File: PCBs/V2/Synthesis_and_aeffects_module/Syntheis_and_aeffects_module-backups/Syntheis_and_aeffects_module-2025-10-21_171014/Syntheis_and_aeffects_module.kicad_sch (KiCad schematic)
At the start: 36 parts, among them J1(AudioJack)1 Conn_01x03, J2(IN)1 IN, J3(OUT)1 OUT, U1 STM32H750VBTx, U2 TPA6110A2DGN

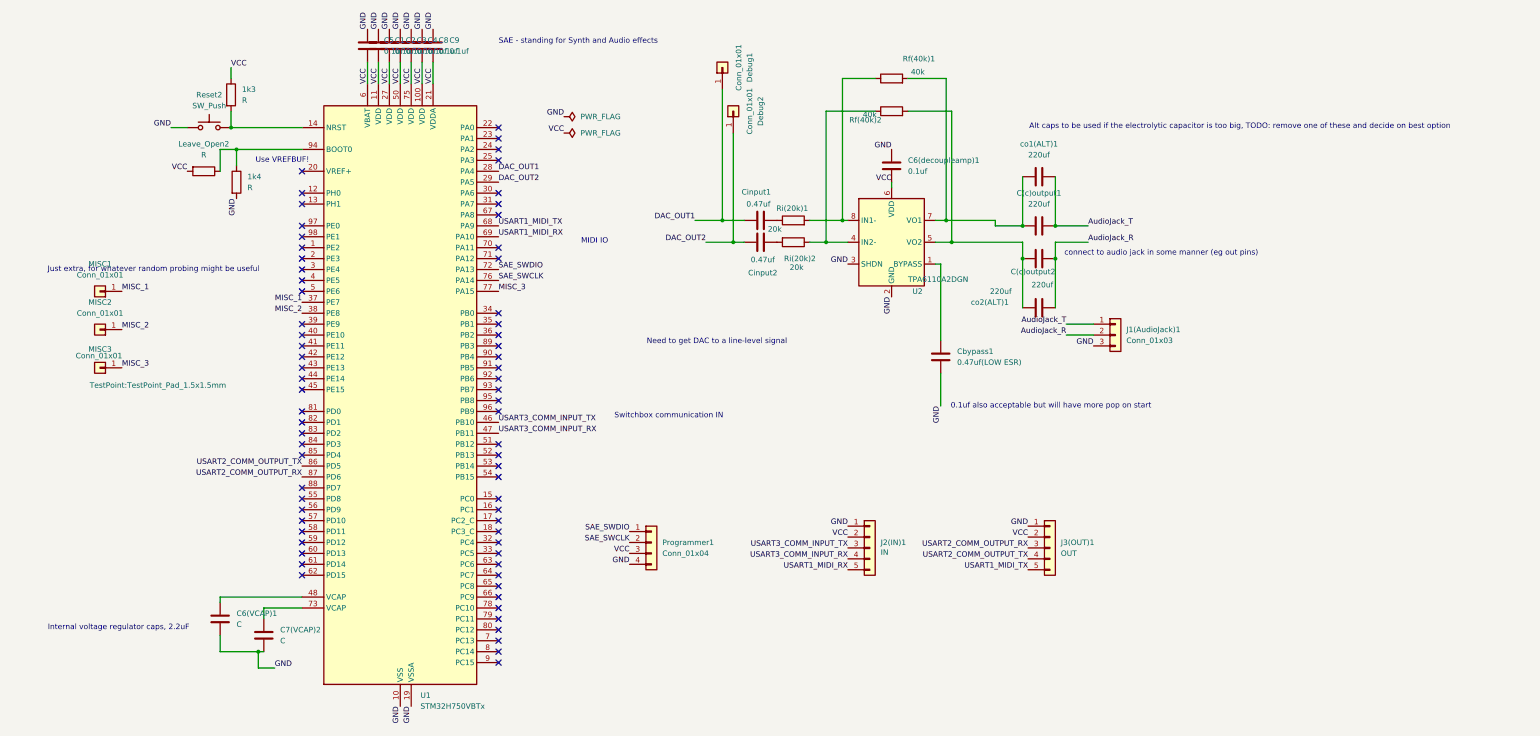
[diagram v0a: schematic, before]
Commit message: testing and fixing PCBs, reordered
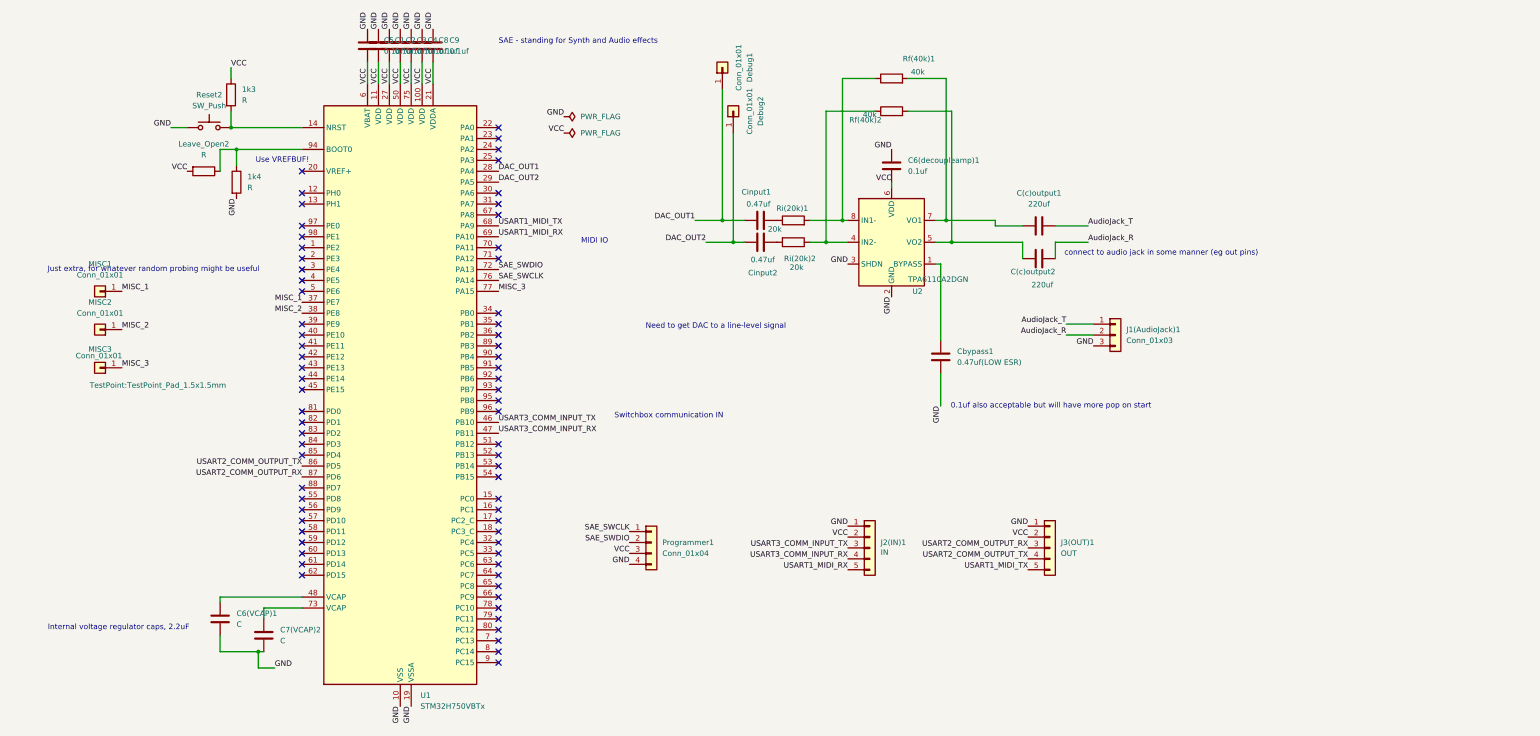
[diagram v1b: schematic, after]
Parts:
- removed co1(ALT)1, co2(ALT)1: 220uf, Capacitor_SMD:C_1206_3216Metric_Pad1.33x1.80mm_HandSolder, symbol Device:C
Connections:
- net SAE_SWCLK: now also Programmer1.1 (Pin_1); no longer Programmer1.2 (Pin_2)
- net SAE_SWDIO: now also Programmer1.2 (Pin_2); no longer Programmer1.1 (Pin_1)
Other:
- note removed: "Alt caps to be used if the electrolytic capacitor is too big, TODO: remove one of these and decide on best option"
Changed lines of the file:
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@@
 	(text "Need to get DAC to a line-level signal"
 		(exclude_from_sim no)
-		(at 176.53 96.774 0)
+		(at 176.276 93.218 0)
 		(effects
 			(font
@@
 		)
 	)
-	(text "Alt caps to be used if the electrolytic capacitor is too big, TODO: remove one of these and decide on best option\n"
-		(exclude_from_sim no)
-		(at 298.196 46.736 0)
-		(effects
-			(font
-				(size 1.27 1.27)
-			)
-		)
-	)
 	(text "Use VREFBUF!\n"
 		(exclude_from_sim no)
@@
 	)
 	(junction
-		(at 255.27 69.85)
-		(diameter 0)
-		(color 0 0 0 0)
-	)
-	(junction
 		(at 63.5 46.99)
 		(diameter 0)
@@
 	)
 	(junction
-		(at 255.27 77.47)
-		(diameter 0)
-		(color 0 0 0 0)
-	)
-	(junction
-		(at 247.65 77.47)
-		(diameter 0)
-		(color 0 0 0 0)
-	)
-	(junction
-		(at 247.65 69.85)
-		(diameter 0)
-		(color 0 0 0 0)
-	)
-	(junction
 		(at 205.74 68.58)
 		(diameter 0)
@@
 	(wire
 		(pts
-			(xy 255.27 58.42) (xy 255.27 69.85)
-		)
-		(stroke
-			(width 0)
-			(type default)
-		)
-	)
-	(wire
-		(pts
 			(xy 227.33 68.58) (xy 229.87 68.58)
 		)
@@
 	(wire
 		(pts
-			(xy 247.65 58.42) (xy 247.65 69.85)
-		)
-		(stroke
-			(width 0)
-			(type default)
-		)
-	)
-	(wire
-		(pts
 			(xy 180.34 73.66) (xy 182.88 73.66)
 		)
@@
 	(wire
 		(pts
-			(xy 247.65 77.47) (xy 247.65 88.9)
-		)
-		(stroke
-			(width 0)
-			(type default)
-		)
-	)
-	(wire
-		(pts
 			(xy 198.12 68.58) (xy 205.74 68.58)
 		)
@@
 	(wire
 		(pts
-			(xy 255.27 77.47) (xy 255.27 88.9)
-		)
-		(stroke
-			(width 0)
-			(type default)
-		)
-	)
-	(wire
-		(pts
 			(xy 173.99 73.66) (xy 180.34 73.66)
 		)
@@
 		)
 	)
+	(label "SAE_SWDIO"
+		(at 156.21 143.51 180)
+		(effects
+			(font
+				(size 1.27 1.27)
+			)
+			(justify right bottom)
+		)
+	)
 	(label "VCC"
 		(at 107.95 36.83 90)
@@
 		)
 	)
-	(label "SAE_SWCLK"
-		(at 156.21 143.51 180)
-		(effects
-			(font
-				(size 1.27 1.27)
-			)
-			(justify right bottom)
-		)
-	)
 	(label "GND"
 		(at 217.17 52.07 180)
@@
 		)
 	)
+	(label "SAE_SWCLK"
+		(at 156.21 140.97 180)
+		(effects
+			(font
+				(size 1.27 1.27)
+			)
+			(justify right bottom)
+		)
+	)
 	(label "DAC_OUT1"
 		(at 171.45 68.58 180)
@@
 		)
 	)
-	(label "SAE_SWDIO"
-		(at 156.21 140.97 180)
-		(effects
-			(font
-				(size 1.27 1.27)
-			)
-			(justify right bottom)
-		)
-	)
-	(symbol
-		(lib_id "Device:C")
-		(at 251.46 88.9 90)
-		(unit 1)
-		(exclude_from_sim no)
-		(in_bom yes)
-		(on_board yes)
-		(dnp no)
-		(property "Reference" "co2(ALT)1"
-			(at 240.03 87.63 90)
-			(effects
-				(font
-					(size 1.27 1.27)
-				)
-			)
-		)
-		(property "Value" "220uf"
-			(at 242.57 85.09 90)
-			(effects
-				(font
-					(size 1.27 1.27)
-				)
-			)
-		)
-		(property "Footprint" "Capacitor_SMD:C_1206_3216Metric_Pad1.33x1.80mm_HandSolder"
-			(at 255.27 87.9348 0)
-			(effects
-				(font
-					(size 1.27 1.27)
-				)
-				(hide yes)
-			)
-		)
-		(property "Datasheet" "~"
-			(at 251.46 88.9 0)
-			(effects
-				(font
-					(size 1.27 1.27)
-				)
-				(hide yes)
-			)
-		)
-		(property "Description" "Unpolarized capacitor"
-			(at 251.46 88.9 0)
-			(effects
-				(font
-					(size 1.27 1.27)
-				)
-				(hide yes)
-			)
-		)
-		(pin "1"
-		)
-		(pin "2"
-		)
-		(instances
-			(project "Syntheis_and_aeffects_module"
-				(path "/edf9ac54-8c23-46ef-867e-bfab8959c07a"
-					(reference "co2(ALT)1")
-					(unit 1)
-				)
-			)
-		)
-	)
 	(symbol
 		(lib_id "Connector_Generic:Conn_01x05")
@@
 					(unit 1)
 				)
-			)
-		)
-	)
-	(symbol
-		(lib_id "Device:C")
-		(at 251.46 58.42 90)
-		(unit 1)
-		(exclude_from_sim no)
-		(in_bom yes)
-		(on_board yes)
-		(dnp no)
-		(fields_autoplaced yes)
-		(property "Reference" "co1(ALT)1"
-			(at 251.46 50.8 90)
-			(effects
-				(font
-					(size 1.27 1.27)
-				)
-			)
-		)
-		(property "Value" "220uf"
-			(at 251.46 53.34 90)
-			(effects
-				(font
-					(size 1.27 1.27)
-				)
-			)
-		)
-		(property "Footprint" "Capacitor_SMD:C_1206_3216Metric_Pad1.33x1.80mm_HandSolder"
-			(at 255.27 57.4548 0)
-			(effects
-				(font
-					(size 1.27 1.27)
-				)
-				(hide yes)
-			)
-		)
-		(property "Datasheet" "~"
-			(at 251.46 58.42 0)
-			(effects
-				(font
-					(size 1.27 1.27)
-				)
-				(hide yes)
-			)
-		)
-		(property "Description" "Unpolarized capacitor"
-			(at 251.46 58.42 0)
-			(effects
-				(font
-					(size 1.27 1.27)
-				)
-				(hide yes)
-			)
-		)
-		(pin "1"
-		)
-		(pin "2"
-		)
-		(instances
-			(project "Syntheis_and_aeffects_module"
-				(path "/edf9ac54-8c23-46ef-867e-bfab8959c07a"
-					(reference "co1(ALT)1")
-					(unit 1)
-				)
